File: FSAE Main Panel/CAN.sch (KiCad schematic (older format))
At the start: 8 parts

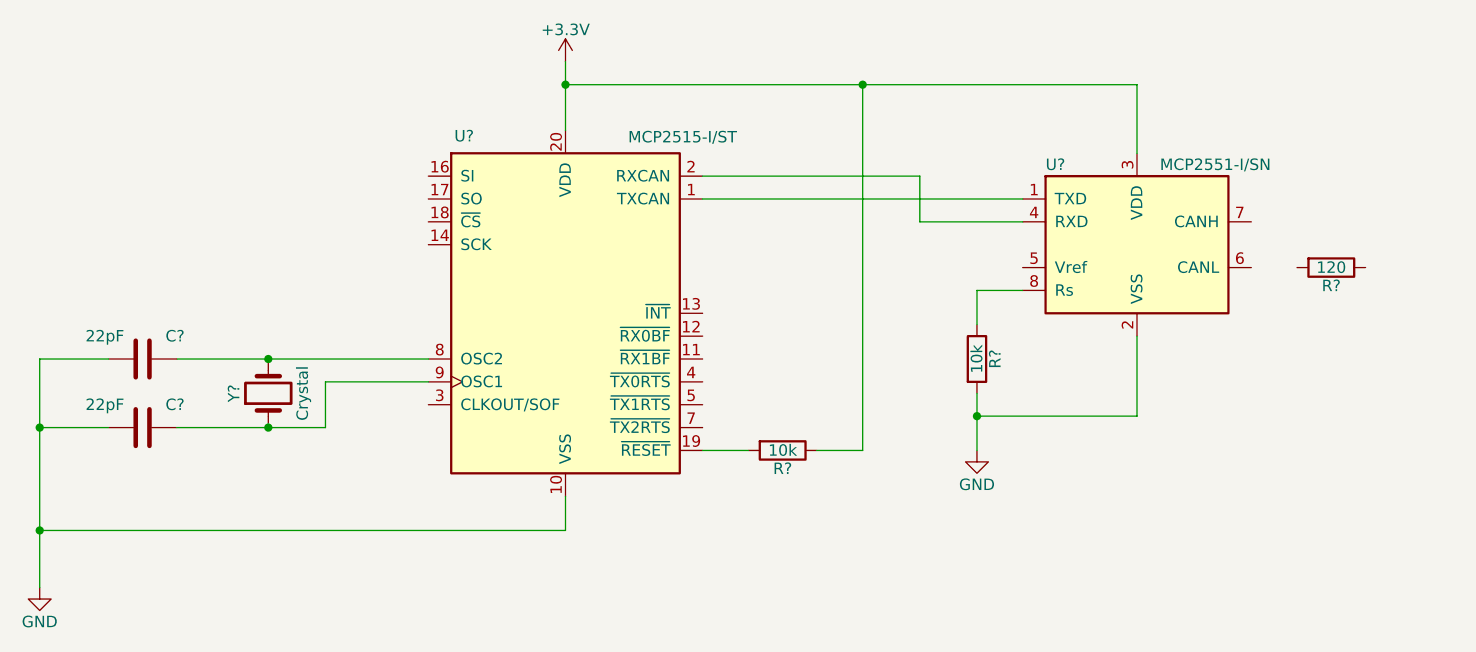
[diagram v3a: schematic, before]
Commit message: Added RPM LED Control
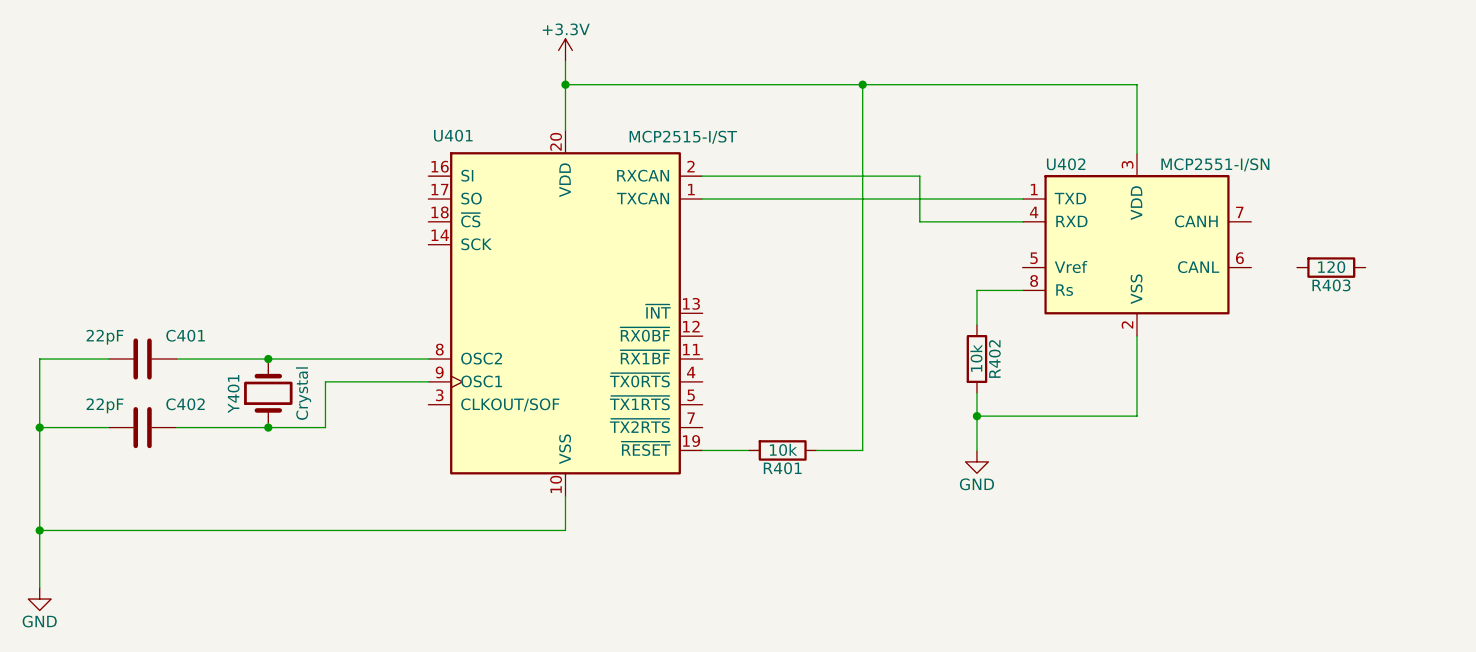
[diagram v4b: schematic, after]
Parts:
- gave numbers to parts that had none: 8
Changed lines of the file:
@@
 LIBS:contrib
 LIBS:valves
+LIBS:TI_Additions
+LIBS:apa102c
+LIBS:KingBright_Addition
+LIBS:lm2734
+LIBS:prtr5v0u2x
+LIBS:samd21g18a-au
 LIBS:FSAE Main Panel-cache
 EELAYER 25 0
@@
 $EndDescr
 $Comp
-L MCP2515-I/ST U?
+L MCP2515-I/ST U401
 U 1 1 5BE2515F
 P 4700 3400
-F 0 "U?" H 4300 4175 50  0000 R CNN
+F 0 "U401" H 4300 4175 50  0000 R CNN
 F 1 "MCP2515-I/ST" H 5450 4200 50  0000 R TNN
 F 2 "Housings_SSOP:TSSOP-20_4.4x6.5mm_Pitch0.65mm" H 4700 2500 50  0001 C CIN
@@
 $EndComp
 $Comp
-L Crystal Y?
+L Crystal Y401
 U 1 1 5BE251BE
 P 3400 3750
-F 0 "Y?" H 3400 3900 50  0000 C CNN
+F 0 "Y401" H 3400 3900 50  0000 C CNN
 F 1 "Crystal" H 3400 3600 50  0000 C CNN
 F 2 "" H 3400 3750 50  0001 C CNN
@@
 	3650 3900 3000 3900
 $Comp
-L C C?
+L C C401
 U 1 1 5BE2525F
 P 2850 3600
-F 0 "C?" V 2750 3700 50  0000 L CNN
+F 0 "C401" V 2750 3700 50  0000 L CNN
 F 1 "22pF" V 2750 3350 50  0000 L CNN
 F 2 "" H 2888 3450 50  0001 C CNN
@@
 $EndComp
 $Comp
-L C C?
+L C C402
 U 1 1 5BE2528F
 P 2850 3900
-F 0 "C?" V 2750 4000 50  0000 L CNN
+F 0 "C402" V 2750 4000 50  0000 L CNN
 F 1 "22pF" V 2750 3650 50  0000 L CNN
 F 2 "" H 2888 3750 50  0001 C CNN
@@
 Connection ~ 3400 3900
 $Comp
-L GND #PWR?
+L GND #PWR401
 U 1 1 5BE2541F
 P 2400 4600
-F 0 "#PWR?" H 2400 4350 50  0001 C CNN
+F 0 "#PWR401" H 2400 4350 50  0001 C CNN
 F 1 "GND" H 2400 4450 50  0000 C CNN
 F 2 "" H 2400 4600 50  0001 C CNN
@@
 Connection ~ 2400 3900
 $Comp
-L +3.3V #PWR?
+L +3.3V #PWR402
 U 1 1 5BE254B2
 P 4700 2300
-F 0 "#PWR?" H 4700 2150 50  0001 C CNN
+F 0 "#PWR402" H 4700 2150 50  0001 C CNN
 F 1 "+3.3V" H 4700 2440 50  0000 C CNN
 F 2 "" H 4700 2300 50  0001 C CNN
@@
 Connection ~ 2400 4350
 $Comp
-L MCP2551-I/SN U?
+L MCP2551-I/SN U402
 U 1 1 5BE25501
 P 7200 3100
-F 0 "U?" H 6800 3450 50  0000 L CNN
+F 0 "U402" H 6800 3450 50  0000 L CNN
 F 1 "MCP2551-I/SN" H 7300 3450 50  0000 L CNN
 F 2 "Housings_SOIC:SOIC-8_3.9x4.9mm_Pitch1.27mm" H 7200 2600 50  0001 C CIN
@@
 	4700 2300 4700 2600
 $Comp
-L R R?
+L R R401
 U 1 1 5BE255B1
 P 5650 4000
-F 0 "R?" V 5730 4000 50  0000 C CNN
+F 0 "R401" V 5730 4000 50  0000 C CNN
 F 1 "10k" V 5650 4000 50  0000 C CNN
 F 2 "" V 5580 4000 50  0001 C CNN
@@
 Connection ~ 4700 2400
 $Comp
-L R R?
+L R R402
 U 1 1 5BE256E6
 P 6500 3600
-F 0 "R?" V 6580 3600 50  0000 C CNN
+F 0 "R402" V 6580 3600 50  0000 C CNN
 F 1 "10k" V 6500 3600 50  0000 C CNN
 F 2 "" V 6430 3600 50  0001 C CNN
@@
 $EndComp
 $Comp
-L GND #PWR?
+L GND #PWR403
 U 1 1 5BE25747
 P 6500 4000
-F 0 "#PWR?" H 6500 3750 50  0001 C CNN
+F 0 "#PWR403" H 6500 3750 50  0001 C CNN
 F 1 "GND" H 6500 3850 50  0000 C CNN
 F 2 "" H 6500 4000 50  0001 C CNN
@@
 Connection ~ 6000 2400
 $Comp
-L R R?
+L R R403
 U 1 1 5BE25A3B
 P 8050 3200
-F 0 "R?" V 8130 3200 50  0000 C CNN
+F 0 "R403" V 8130 3200 50  0000 C CNN
 F 1 "120" V 8050 3200 50  0000 C CNN
 F 2 "" V 7980 3200 50  0001 C CNN

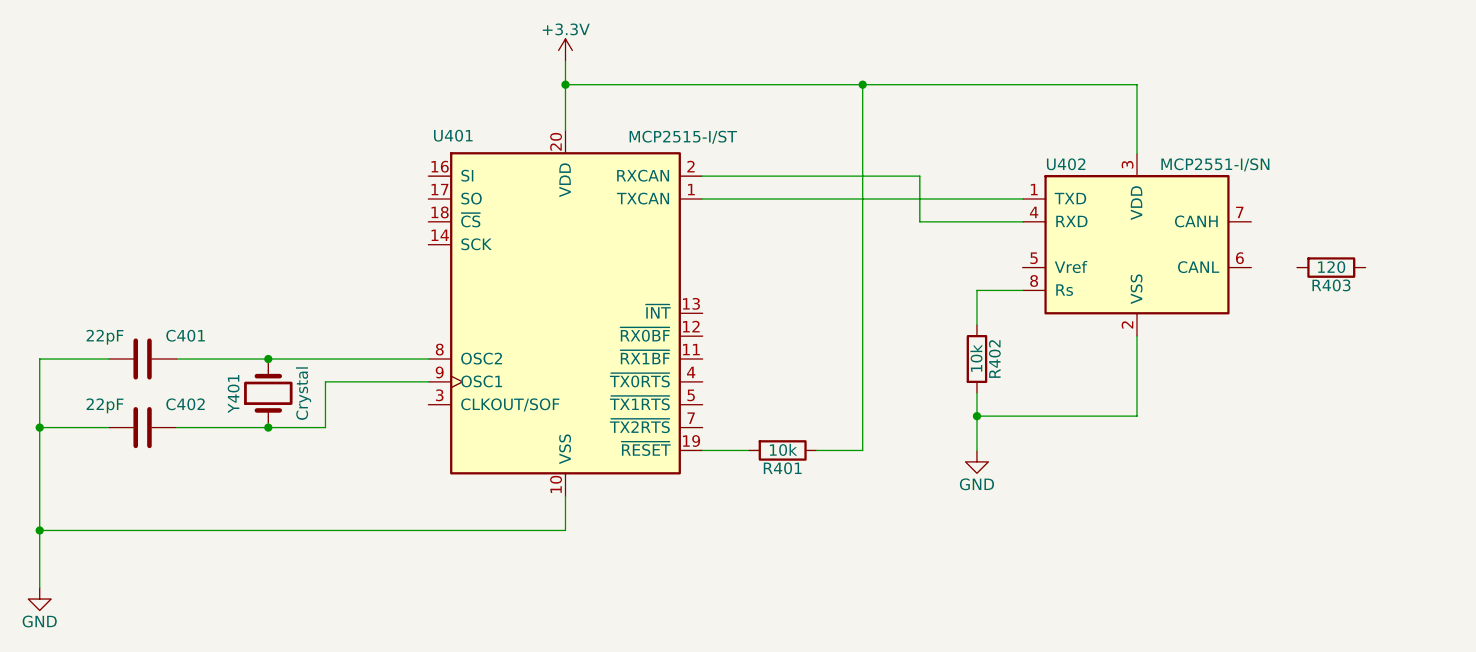
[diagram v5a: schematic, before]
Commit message: Cortex debugger, GPIO pinning, minor fixes
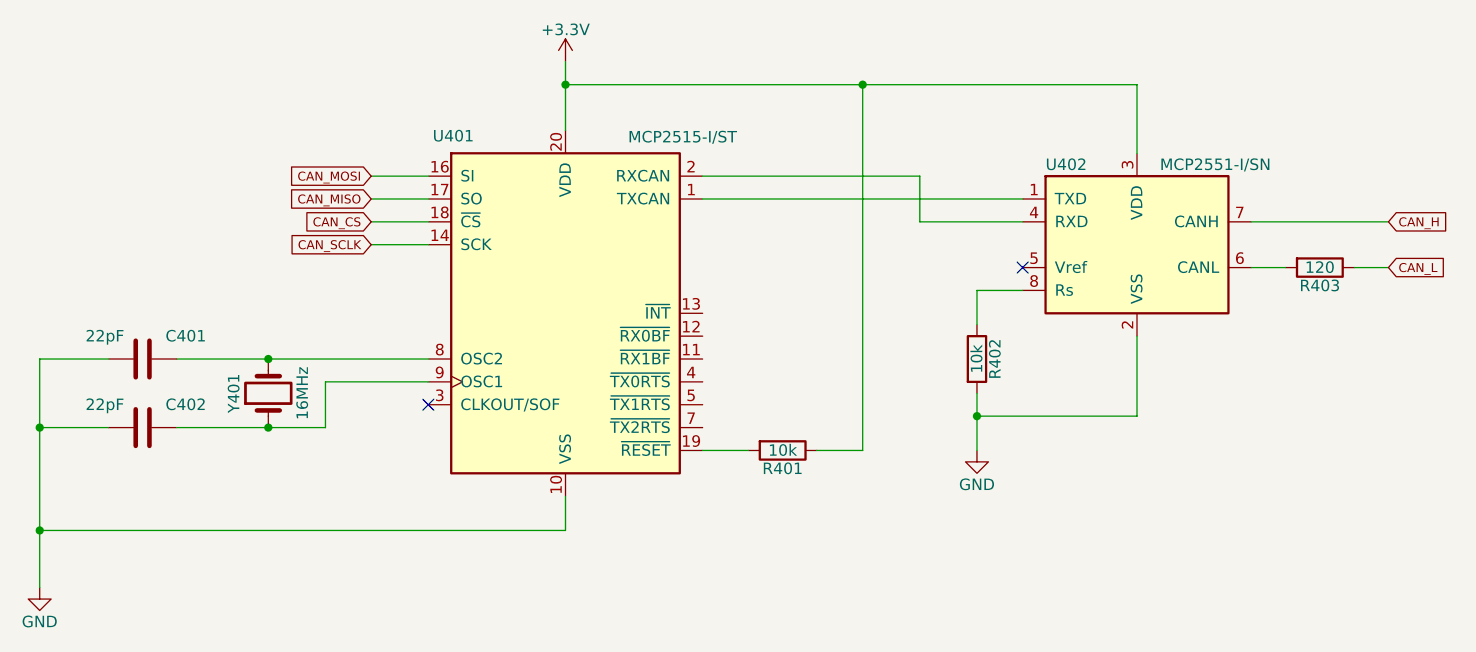
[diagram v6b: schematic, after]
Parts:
- Y401: value Crystal -> 16MHz
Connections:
- net CAN_SCLK: now reaches U401.14 (SCK)
- net CAN_MOSI: now reaches U401.16 (SI)
- net CAN_MISO: now reaches U401.17 (SO)
- net CAN_CS: now reaches U401.18 (~CS)
- net at U402.6 (CANL): now also R403.2
- net CAN_H: now reaches U402.7 (CANH)
- net CAN_L: now reaches R403.1
- no-connect marks 0 -> 2
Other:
- moved on the sheet: R403
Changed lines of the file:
@@
 LIBS:samd21g18a-au
 LIBS:zldo1117-5v
+LIBS:cortex_debug
 LIBS:FSAE Main Panel-cache
 EELAYER 25 0
@@
 P 3400 3750
 F 0 "Y401" H 3400 3900 50  0000 C CNN
-F 1 "Crystal" H 3400 3600 50  0000 C CNN
+F 1 "16MHz" H 3400 3600 50  0000 C CNN
 F 2 "" H 3400 3750 50  0001 C CNN
 F 3 "" H 3400 3750 50  0001 C CNN
@@
 L R R403
 U 1 1 5BE25A3B
-P 8050 3200
-F 0 "R403" V 8130 3200 50  0000 C CNN
-F 1 "120" V 8050 3200 50  0000 C CNN
-F 2 "" V 7980 3200 50  0001 C CNN
-F 3 "" H 8050 3200 50  0001 C CNN
-	1    8050 3200
-	0    1    1    0
-$EndComp
+P 8000 3200
+F 0 "R403" V 8080 3200 50  0000 C CNN
+F 1 "120" V 8000 3200 50  0000 C CNN
+F 2 "" V 7930 3200 50  0001 C CNN
+F 3 "" H 8000 3200 50  0001 C CNN
+	1    8000 3200
+	0    1    1    0
+$EndComp
+Text GLabel 8300 3000 2    39   Input ~ 0
+CAN_H
+Text GLabel 8300 3200 2    39   Input ~ 0
+CAN_L
+Wire Wire Line
+	7700 3000 8300 3000
+Wire Wire Line
+	7700 3200 7850 3200
+Wire Wire Line
+	8150 3200 8300 3200
+Text GLabel 3850 3100 0    39   Input ~ 0
+CAN_SCLK
+Text GLabel 3850 3000 0    39   Input ~ 0
+CAN_CS
+Text GLabel 3850 2900 0    39   Input ~ 0
+CAN_MISO
+Text GLabel 3850 2800 0    39   Input ~ 0
+CAN_MOSI
+Wire Wire Line
+	3850 2800 4100 2800
+Wire Wire Line
+	4100 2900 3850 2900
+Wire Wire Line
+	3850 3000 4100 3000
+Wire Wire Line
+	4100 3100 3850 3100
+NoConn ~ 6700 3200
+NoConn ~ 4100 3800
 $EndSCHEMATC

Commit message: Updated to KiCad 5
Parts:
- C401, C402: symbol C -> Device:C
- R401, R402, R403: symbol R -> Device:R
- U401: symbol MCP2515-I/ST -> FSAE-Main-Panel-rescue:MCP2515-I_ST
- U402: symbol MCP2551-I/SN -> FSAE-Main-Panel-rescue:MCP2551-I_SN
- Y401: symbol Crystal -> Device:Crystal
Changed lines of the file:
@@
-EESchema Schematic File Version 2
-LIBS:power
-LIBS:device
-LIBS:switches
-LIBS:relays
-LIBS:motors
-LIBS:transistors
-LIBS:conn
-LIBS:linear
-LIBS:regul
-LIBS:74xx
-LIBS:cmos4000
-LIBS:adc-dac
-LIBS:memory
-LIBS:xilinx
-LIBS:microcontrollers
-LIBS:dsp
-LIBS:microchip
-LIBS:analog_switches
-LIBS:motorola
-LIBS:texas
-LIBS:intel
-LIBS:audio
-LIBS:interface
-LIBS:digital-audio
-LIBS:philips
-LIBS:display
-LIBS:cypress
-LIBS:siliconi
-LIBS:opto
-LIBS:atmel
-LIBS:contrib
-LIBS:valves
-LIBS:TI_Additions
-LIBS:KingBright_Addition
-LIBS:lm2734
-LIBS:prtr5v0u2x
-LIBS:samd21g18a-au
-LIBS:zldo1117-5v
-LIBS:cortex_debug
+EESchema Schematic File Version 4
 LIBS:FSAE Main Panel-cache
-EELAYER 25 0
+EELAYER 26 0
 EELAYER END
 $Descr A4 11693 8268
@@
 $EndDescr
 $Comp
-L MCP2515-I/ST U401
+L FSAE-Main-Panel-rescue:MCP2515-I_ST U401
 U 1 1 5BE2515F
 P 4700 3400
@@
 $EndComp
 $Comp
-L Crystal Y401
+L Device:Crystal Y401
 U 1 1 5BE251BE
 P 3400 3750
@@
 	3650 3900 3000 3900
 $Comp
-L C C401
+L Device:C C401
 U 1 1 5BE2525F
 P 2850 3600
@@
 $EndComp
 $Comp
-L C C402
+L Device:C C402
 U 1 1 5BE2528F
 P 2850 3900
@@
 Connection ~ 3400 3900
 $Comp
-L GND #PWR401
+L power:GND #PWR401
 U 1 1 5BE2541F
 P 2400 4600
@@
 Connection ~ 2400 3900
 $Comp
-L +3.3V #PWR402
+L power:+3.3V #PWR402
 U 1 1 5BE254B2
 P 4700 2300
@@
 Connection ~ 2400 4350
 $Comp
-L MCP2551-I/SN U402
+L FSAE-Main-Panel-rescue:MCP2551-I_SN U402
 U 1 1 5BE25501
 P 7200 3100
@@
 	4700 2300 4700 2600
 $Comp
-L R R401
+L Device:R R401
 U 1 1 5BE255B1
 P 5650 4000
@@
 Connection ~ 4700 2400
 $Comp
-L R R402
+L Device:R R402
 U 1 1 5BE256E6
 P 6500 3600
@@
 $EndComp
 $Comp
-L GND #PWR403
+L power:GND #PWR403
 U 1 1 5BE25747
 P 6500 4000
@@
 Connection ~ 6000 2400
 $Comp
-L R R403
+L Device:R R403
 U 1 1 5BE25A3B
 P 8000 3200

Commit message: Updated Footprint Association
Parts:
- C401, C402: footprint (none) -> Capacitors_SMD:C_1206; Description (none) -> Ceramic 22pF 10V C0G/NG0 0805
- R401, R402, R403: footprint (none) -> Resistors_SMD:R_1206
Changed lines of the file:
@@
 $EndComp
 Wire Wire Line
-	3000 3600 4100 3600
+	3000 3600 3400 3600
 Wire Wire Line
 	4100 3700 3650 3700
@@
 	3650 3700 3650 3900
 Wire Wire Line
-	3650 3900 3000 3900
+	3650 3900 3400 3900
 $Comp
 L Device:C C401
@@
 F 0 "C401" V 2750 3700 50  0000 L CNN
 F 1 "22pF" V 2750 3350 50  0000 L CNN
-F 2 "" H 2888 3450 50  0001 C CNN
+F 2 "Capacitors_SMD:C_1206" H 2888 3450 50  0001 C CNN
 F 3 "" H 2850 3600 50  0001 C CNN
+F 4 "Ceramic 22pF 10V C0G/NG0 0805" V 2850 3600 50  0001 C CNN "Description"
 	1    2850 3600
 	0    1    1    0
@@
 F 0 "C402" V 2750 4000 50  0000 L CNN
 F 1 "22pF" V 2750 3650 50  0000 L CNN
-F 2 "" H 2888 3750 50  0001 C CNN
+F 2 "Capacitors_SMD:C_1206" H 2888 3750 50  0001 C CNN
 F 3 "" H 2850 3900 50  0001 C CNN
+F 4 "Ceramic 22pF 10V C0G/NG0 0805" V 2850 3900 50  0001 C CNN "Description"
 	1    2850 3900
 	0    1    1    0
@@
 Connection ~ 3400 3900
 $Comp
-L power:GND #PWR401
+L power:GND #PWR0401
 U 1 1 5BE2541F
 P 2400 4600
-F 0 "#PWR401" H 2400 4350 50  0001 C CNN
+F 0 "#PWR0401" H 2400 4350 50  0001 C CNN
 F 1 "GND" H 2400 4450 50  0000 C CNN
 F 2 "" H 2400 4600 50  0001 C CNN
@@
 	2700 3600 2400 3600
 Wire Wire Line
-	2400 3600 2400 4600
+	2400 3600 2400 3900
 Wire Wire Line
 	2700 3900 2400 3900
 Connection ~ 2400 3900
 $Comp
-L power:+3.3V #PWR402
+L power:+3.3V #PWR0402
 U 1 1 5BE254B2
 P 4700 2300
-F 0 "#PWR402" H 4700 2150 50  0001 C CNN
+F 0 "#PWR0402" H 4700 2150 50  0001 C CNN
 F 1 "+3.3V" H 4700 2440 50  0000 C CNN
 F 2 "" H 4700 2300 50  0001 C CNN
@@
 $EndComp
 Wire Wire Line
-	4700 2300 4700 2600
+	4700 2300 4700 2400
 $Comp
 L Device:R R401
@@
 F 0 "R401" V 5730 4000 50  0000 C CNN
 F 1 "10k" V 5650 4000 50  0000 C CNN
-F 2 "" V 5580 4000 50  0001 C CNN
+F 2 "Resistors_SMD:R_1206" V 5580 4000 50  0001 C CNN
 F 3 "" H 5650 4000 50  0001 C CNN
 	1    5650 4000
@@
 	6000 4000 6000 2400
 Wire Wire Line
-	4700 2400 7200 2400
+	4700 2400 6000 2400
 Connection ~ 4700 2400
 $Comp
@@
 F 0 "R402" V 6580 3600 50  0000 C CNN
 F 1 "10k" V 6500 3600 50  0000 C CNN
-F 2 "" V 6430 3600 50  0001 C CNN
+F 2 "Resistors_SMD:R_1206" V 6430 3600 50  0001 C CNN
 F 3 "" H 6500 3600 50  0001 C CNN
 	1    6500 3600
@@
 $EndComp
 $Comp
-L power:GND #PWR403
+L power:GND #PWR0403
 U 1 1 5BE25747
 P 6500 4000
-F 0 "#PWR403" H 6500 3750 50  0001 C CNN
+F 0 "#PWR0403" H 6500 3750 50  0001 C CNN
 F 1 "GND" H 6500 3850 50  0000 C CNN
 F 2 "" H 6500 4000 50  0001 C CNN
@@
 	6500 3300 6500 3450
 Wire Wire Line
-	6500 3750 6500 4000
+	6500 3750 6500 3850
 Wire Wire Line
 	7200 3500 7200 3850
@@
 F 0 "R403" V 8080 3200 50  0000 C CNN
 F 1 "120" V 8000 3200 50  0000 C CNN
-F 2 "" V 7930 3200 50  0001 C CNN
+F 2 "Resistors_SMD:R_1206" V 7930 3200 50  0001 C CNN
 F 3 "" H 8000 3200 50  0001 C CNN
 	1    8000 3200
@@
 NoConn ~ 6700 3200
 NoConn ~ 4100 3800
+Wire Wire Line
+	3400 3600 4100 3600
+Wire Wire Line
+	3400 3900 3000 3900
+Wire Wire Line
+	2400 3900 2400 4350
+Wire Wire Line
+	2400 4350 2400 4600
+Wire Wire Line
+	4700 2400 4700 2600
+Wire Wire Line
+	6500 3850 6500 4000
+Wire Wire Line
+	6000 2400 7200 2400
 $EndSCHEMATC
